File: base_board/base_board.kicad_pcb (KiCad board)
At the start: 6 copper layers, 50 x 50 mm, 62 parts, among them J1 Conn_ARM_JTAG_SWD_20, J3 Conn_01x04, SW1 SW_Push, U1 STM32F446ZEJx, U2 IS42S16400J-xT, U3 BMI270, U4 USB_C_Receptacle_USB2.0, U5 10p, U6 10p, U7 LD3985M33R_SOT23, Y1 Crystal_GND24

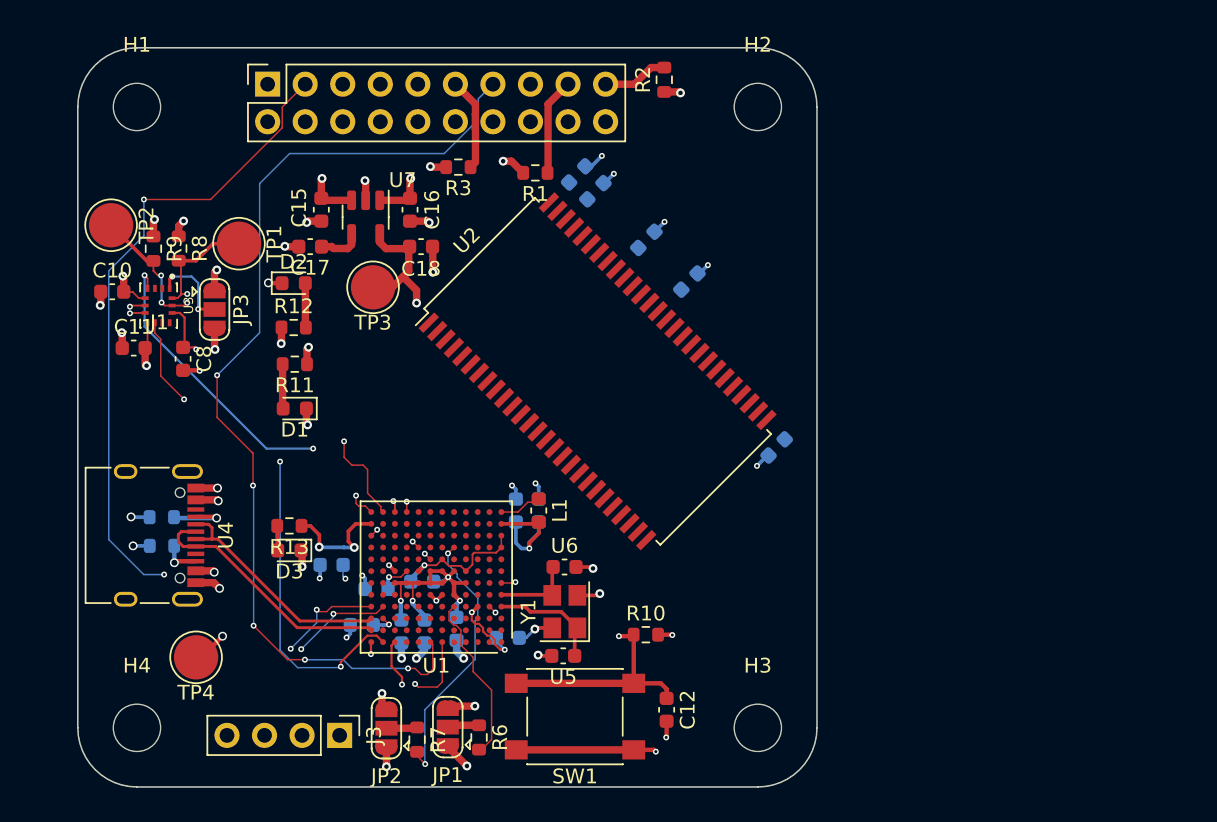
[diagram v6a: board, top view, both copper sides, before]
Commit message: [pcb] moved sdram chip to the same layer with mcu
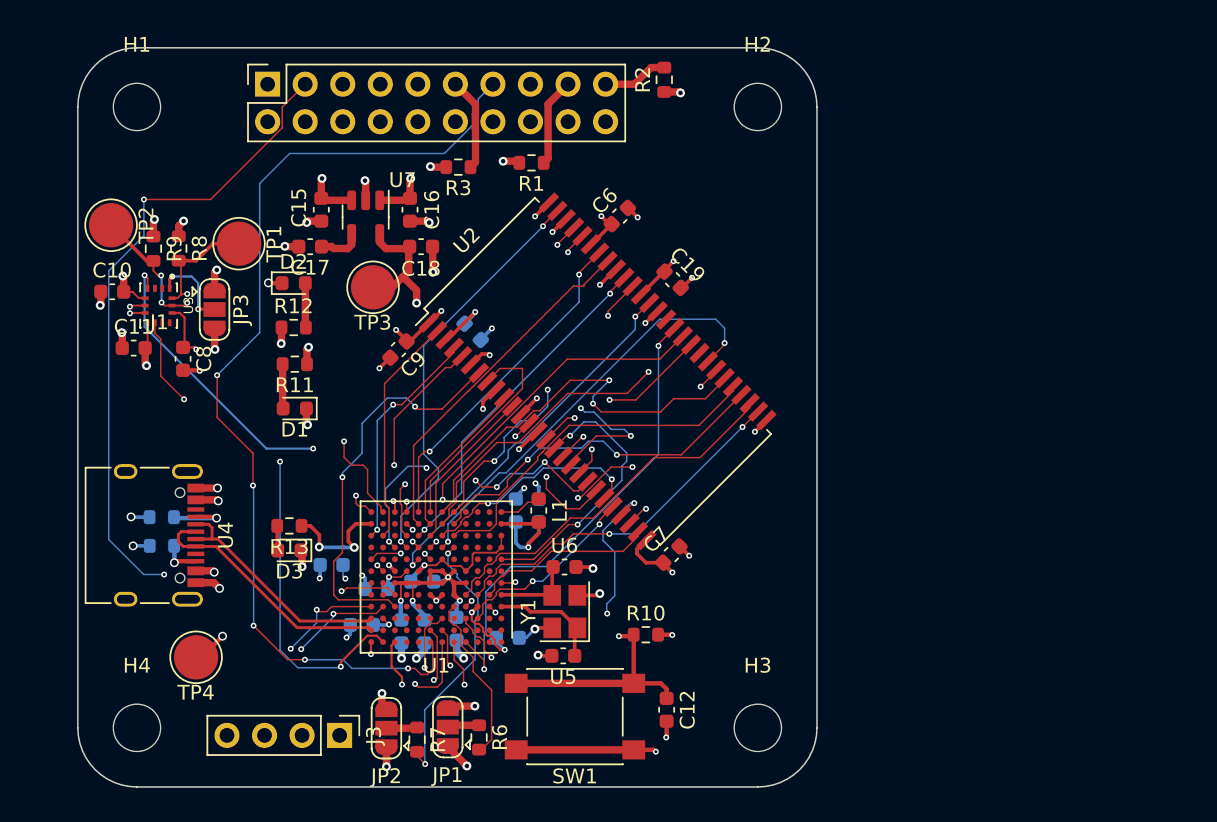
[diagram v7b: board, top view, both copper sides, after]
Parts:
- C19, C6, C7, C9: moved to F.Cu
- moved C9 18.3 mm to (124.7, 88.4), turned to -135 degrees
- moved C5 12.8 mm to (129.7, 87.2), turned to -45 degrees
- moved C7 10.2 mm to (143.2, 102.3), turned to 45 degrees
- moved C6 2.35 mm to (139.7, 79.4)
- moved C19 1.14 mm to (143.2, 83.7), turned to -45 degrees
- moved R1 0.73 mm to (133.7, 75.8)
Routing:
- net /FMC_SDKE1: track 0.00 -> 32.8 mm, vias 0 -> 2
- net /FMC_NBL1: track 0.00 -> 32.2 mm, vias 0 -> 2
- net /FMC_NBL0: track 0.00 -> 30.9 mm, vias 0 -> 2
- net /FMC_SDNE1: track 0.00 -> 30.2 mm, vias 0 -> 2
- net /FMC_SDCLK: track 0.00 -> 29.3 mm, vias 0 -> 2
- net /FMC_A11: track 0.00 -> 29.2 mm, vias 0 -> 2
- net /FMC_D15: track 0.00 -> 28.2 mm, vias 0 -> 2
- net /FMC_A8: track 0.38 -> 28.0 mm, vias 0 -> 2
- net /FMC_D2: track 0.00 -> 27.4 mm, vias 0 -> 2
- net /FMC_D13: track 0.00 -> 26.8 mm, vias 0 -> 2
- net /FMC_D3: track 0.00 -> 26.8 mm, vias 0 -> 2
- net /FMC_SDNCAS: track 0.00 -> 26.3 mm, vias 0 -> 2
- net /FMC_D14: track 0.00 -> 25.9 mm, vias 0 -> 2
- net /FMC_A5: track 0.00 -> 25.4 mm
- net /FMC_D8: track 0.00 -> 25.2 mm, vias 0 -> 2
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
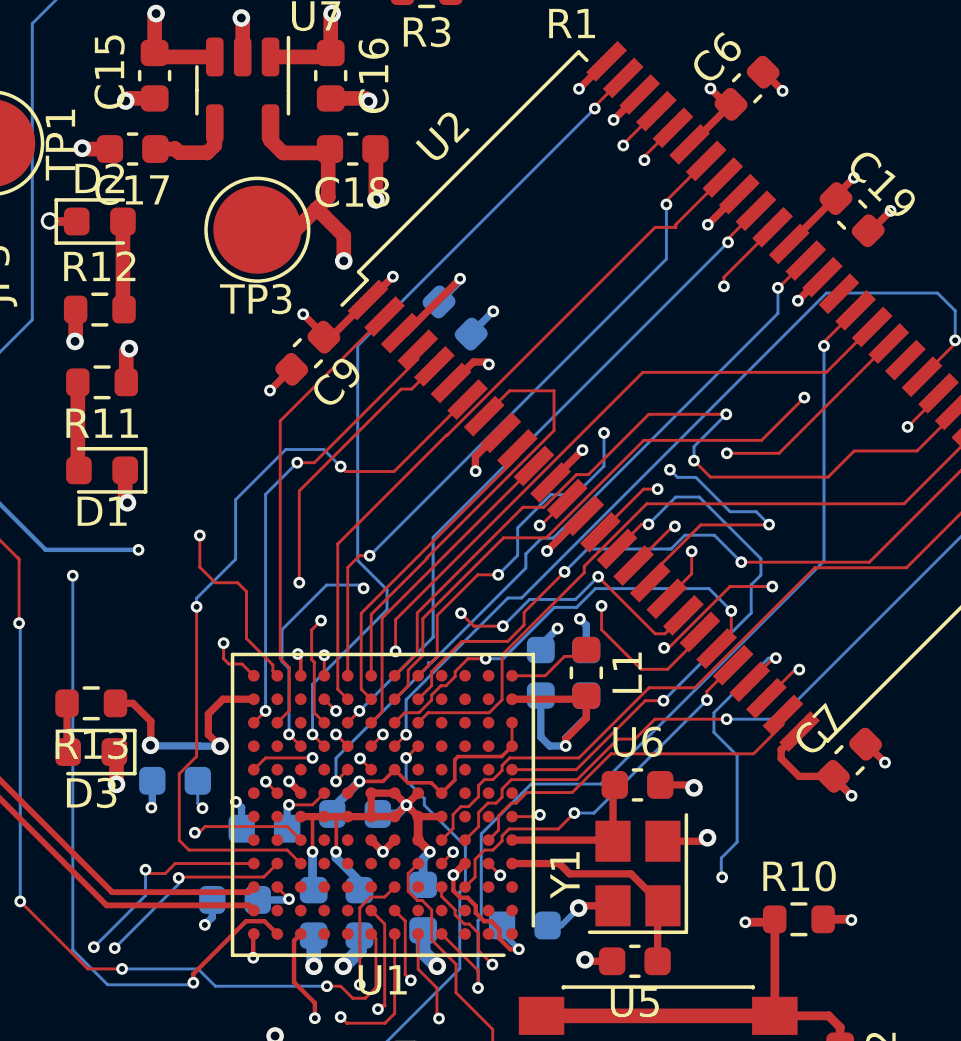
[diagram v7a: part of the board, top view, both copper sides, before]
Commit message: [pcb] draft of length matching implementation
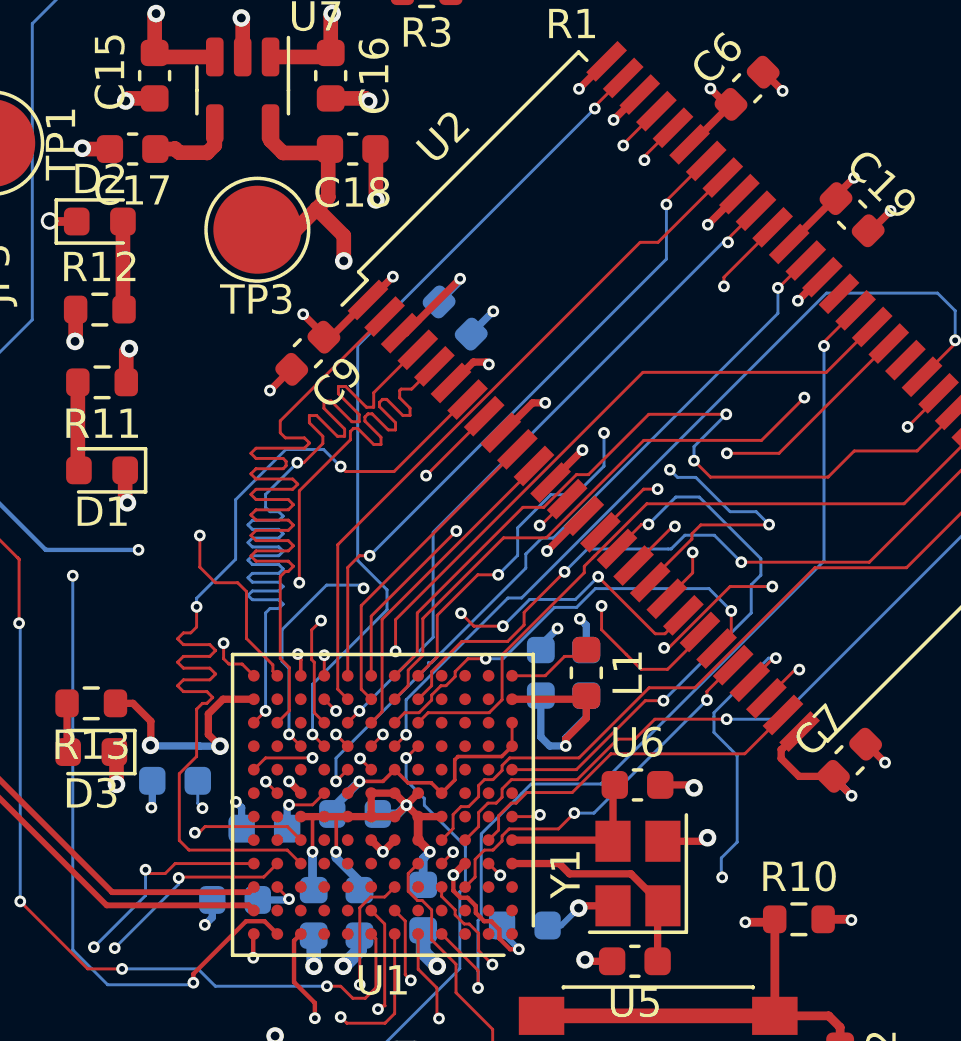
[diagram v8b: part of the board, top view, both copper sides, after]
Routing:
- net /FMC_D1: track 15.4 -> 33.0 mm
- net /FMC_D0: track 15.6 -> 32.0 mm
- net /FMC_D3: track 26.8 -> 32.8 mm
- net /FMC_D2: track 27.4 -> 32.6 mm
- net /FMC_D4: track 15.0 -> 11.3 mm, vias 0 -> 2
- net /FMC_D13: track 26.8 -> 26.2 mm
